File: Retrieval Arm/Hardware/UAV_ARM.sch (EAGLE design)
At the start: 20 parts, among them Q1 Q_ATMEGA328P, Q2 Q_LTC490, Q3 Q_LDO, X1 X_HC49SCRYSTAL

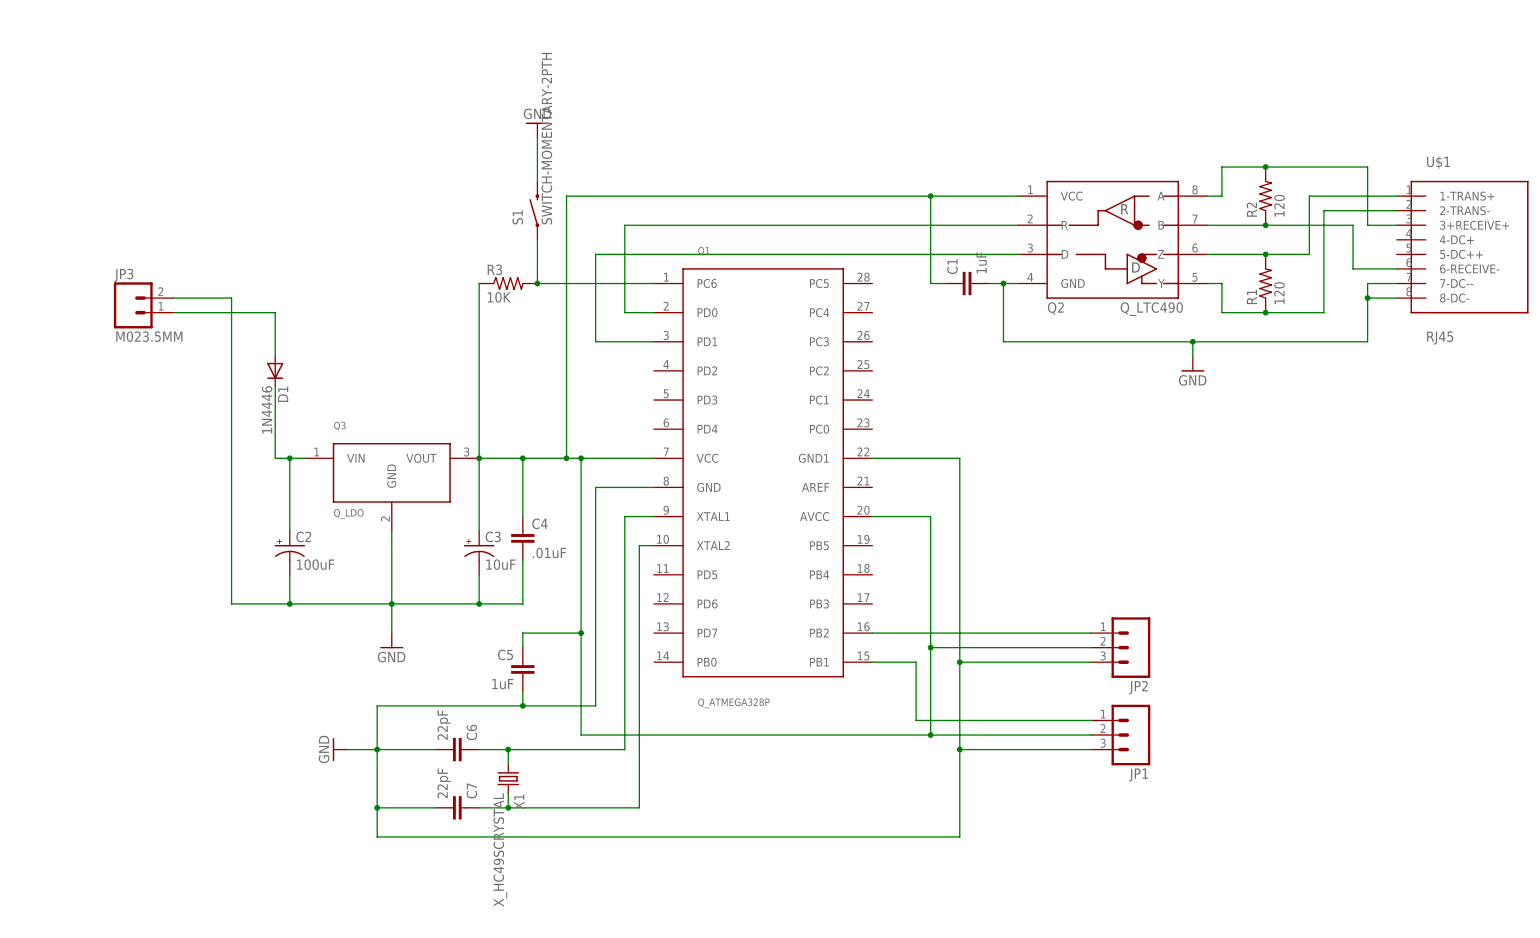
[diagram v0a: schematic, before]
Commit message: Redesigned for new arm
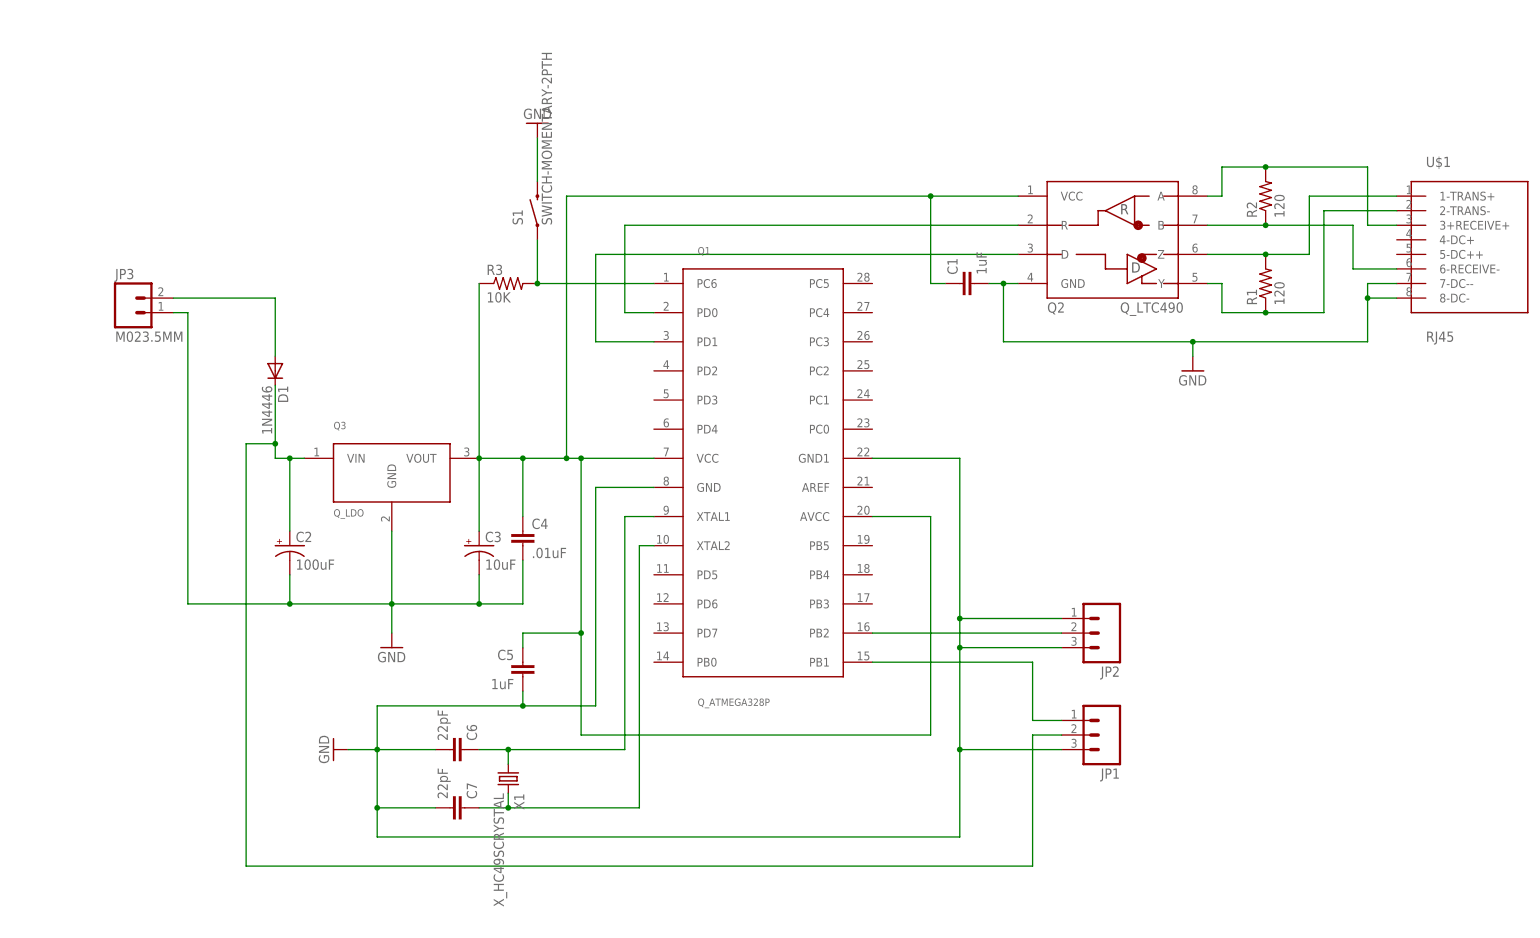
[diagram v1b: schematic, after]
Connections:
- removed net N$12: JP2.1, Q1.PB2
- removed net N$14 (its old number): C1.1, C3.+, C4.1, C5.1, JP1.2, JP2.2, Q1.AVCC, Q1.VCC, Q2.VCC, Q3.VOUT, R3.1
- new net N$15: D1.A, JP3.2
- new net N$6: C1.1, C3.+, C4.1, C5.1, Q1.AVCC, Q1.VCC, Q2.VCC, Q3.VOUT, R3.1
- net GND: now also JP2.1, JP3.1; no longer JP3.2
- net N$13: now also JP2.2, Q1.PB2; no longer D1.A, JP3.1
- net N$5: now also JP1.2
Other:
- moved on the sheet: JP1, JP2
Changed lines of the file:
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@@
 <part name="X1" library="MRDT-2014-All" deviceset="X_HC49SCRYSTAL" device=""/>
 <part name="GND4" library="supply1" deviceset="GND" device=""/>
+<part name="JP3" library="SparkFun-Connectors" deviceset="M02" device="3.5MM"/>
+<part name="S1" library="SparkFun-Electromechanical" deviceset="SWITCH-MOMENTARY-2" device="PTH"/>
 <part name="JP1" library="SparkFun-Connectors" deviceset="M03" device="POLAR"/>
 <part name="JP2" library="SparkFun-Connectors" deviceset="M03" device="POLAR"/>
-<part name="JP3" library="SparkFun-Connectors" deviceset="M02" device="3.5MM"/>
-<part name="S1" library="SparkFun-Electromechanical" deviceset="SWITCH-MOMENTARY-2" device="PTH"/>
 </parts>
 <sheets>
@@
 <instance part="X1" gate="G$1" x="43.18" y="-20.32" rot="R270"/>
 <instance part="GND4" gate="1" x="12.7" y="-15.24" rot="R270"/>
-<instance part="JP1" gate="G$1" x="152.4" y="-12.7" rot="R180"/>
-<instance part="JP2" gate="G$1" x="152.4" y="2.54" rot="R180"/>
 <instance part="JP3" gate="G$1" x="-22.86" y="60.96"/>
 <instance part="S1" gate="G$1" x="48.26" y="78.74" rot="R90"/>
+<instance part="JP1" gate="G$1" x="147.32" y="-12.7" rot="R180"/>
+<instance part="JP2" gate="G$1" x="147.32" y="5.08" rot="R180"/>
 </instances>
 <busses>
@@
 <junction x="38.1" y="10.16"/>
 <junction x="22.86" y="10.16"/>
-<wire x1="5.08" y1="10.16" x2="-5.08" y2="10.16" width="0.1524" layer="91"/>
-<wire x1="-5.08" y1="10.16" x2="-5.08" y2="63.5" width="0.1524" layer="91"/>
-<pinref part="JP3" gate="G$1" pin="2"/>
-<wire x1="-15.24" y1="63.5" x2="-5.08" y2="63.5" width="0.1524" layer="91"/>
+<wire x1="5.08" y1="10.16" x2="-12.7" y2="10.16" width="0.1524" layer="91"/>
 <junction x="5.08" y="10.16"/>
+<wire x1="-12.7" y1="10.16" x2="-12.7" y2="60.96" width="0.1524" layer="91"/>
+<pinref part="JP3" gate="G$1" pin="1"/>
+<wire x1="-12.7" y1="60.96" x2="-15.24" y2="60.96" width="0.1524" layer="91"/>
 </segment>
 <segment>
@@
 <pinref part="Q1" gate="G$1" pin="GND1"/>
 <wire x1="106.68" y1="35.56" x2="121.92" y2="35.56" width="0.1524" layer="91"/>
-<wire x1="121.92" y1="35.56" x2="121.92" y2="0" width="0.1524" layer="91"/>
-<wire x1="121.92" y1="0" x2="121.92" y2="-15.24" width="0.1524" layer="91"/>
+<wire x1="121.92" y1="35.56" x2="121.92" y2="7.62" width="0.1524" layer="91"/>
+<wire x1="121.92" y1="7.62" x2="121.92" y2="2.54" width="0.1524" layer="91"/>
+<wire x1="121.92" y1="2.54" x2="121.92" y2="-15.24" width="0.1524" layer="91"/>
 <wire x1="121.92" y1="-15.24" x2="121.92" y2="-30.48" width="0.1524" layer="91"/>
 <wire x1="121.92" y1="-30.48" x2="20.32" y2="-30.48" width="0.1524" layer="91"/>
 <wire x1="20.32" y1="-30.48" x2="20.32" y2="-25.4" width="0.1524" layer="91"/>
 <junction x="20.32" y="-25.4"/>
-<pinref part="JP2" gate="G$1" pin="3"/>
-<wire x1="144.78" y1="0" x2="121.92" y2="0" width="0.1524" layer="91"/>
-<pinref part="JP1" gate="G$1" pin="3"/>
-<wire x1="144.78" y1="-15.24" x2="121.92" y2="-15.24" width="0.1524" layer="91"/>
-<junction x="121.92" y="-15.24"/>
-<junction x="121.92" y="0"/>
 <pinref part="C5" gate="G$1" pin="2"/>
 <wire x1="20.32" y1="-7.62" x2="45.72" y2="-7.62" width="0.1524" layer="91"/>
@@
 <wire x1="45.72" y1="-7.62" x2="58.42" y2="-7.62" width="0.1524" layer="91"/>
 <junction x="45.72" y="-7.62"/>
-</segment>
-</net>
-<net name="N$5" class="0">
-<segment>
-<pinref part="Q3" gate="G$1" pin="VIN"/>
-<pinref part="D1" gate="1" pin="C"/>
-<wire x1="7.62" y1="35.56" x2="5.08" y2="35.56" width="0.1524" layer="91"/>
-<wire x1="5.08" y1="35.56" x2="2.54" y2="35.56" width="0.1524" layer="91"/>
-<wire x1="2.54" y1="35.56" x2="2.54" y2="48.26" width="0.1524" layer="91"/>
-<pinref part="C2" gate="G$1" pin="+"/>
-<wire x1="5.08" y1="22.86" x2="5.08" y2="35.56" width="0.1524" layer="91"/>
-<junction x="5.08" y="35.56"/>
+<wire x1="139.7" y1="-15.24" x2="121.92" y2="-15.24" width="0.1524" layer="91"/>
+<junction x="121.92" y="-15.24"/>
+<pinref part="JP1" gate="G$1" pin="3"/>
+<wire x1="139.7" y1="2.54" x2="121.92" y2="2.54" width="0.1524" layer="91"/>
+<pinref part="JP2" gate="G$1" pin="1"/>
+<wire x1="139.7" y1="7.62" x2="121.92" y2="7.62" width="0.1524" layer="91"/>
+<junction x="121.92" y="2.54"/>
+<junction x="121.92" y="7.62"/>
+<pinref part="JP2" gate="G$1" pin="3"/>
 </segment>
 </net>
@@
 </segment>
 </net>
-<net name="N$16" class="0">
-<segment>
-<pinref part="JP1" gate="G$1" pin="1"/>
-<wire x1="144.78" y1="-10.16" x2="114.3" y2="-10.16" width="0.1524" layer="91"/>
-<wire x1="114.3" y1="-10.16" x2="114.3" y2="0" width="0.1524" layer="91"/>
-<pinref part="Q1" gate="G$1" pin="PB1"/>
-<wire x1="114.3" y1="0" x2="106.68" y2="0" width="0.1524" layer="91"/>
-</segment>
-</net>
-<net name="N$12" class="0">
-<segment>
-<pinref part="JP2" gate="G$1" pin="1"/>
-<pinref part="Q1" gate="G$1" pin="PB2"/>
-<wire x1="144.78" y1="5.08" x2="106.68" y2="5.08" width="0.1524" layer="91"/>
-</segment>
-</net>
-<net name="N$13" class="0">
-<segment>
-<pinref part="D1" gate="1" pin="A"/>
-<wire x1="-15.24" y1="60.96" x2="2.54" y2="60.96" width="0.1524" layer="91"/>
-<wire x1="2.54" y1="60.96" x2="2.54" y2="53.34" width="0.1524" layer="91"/>
-<pinref part="JP3" gate="G$1" pin="1"/>
-</segment>
-</net>
 <net name="N$8" class="0">
 <segment>
@@
 </segment>
 </net>
-<net name="N$14" class="0">
+<net name="N$6" class="0">
 <segment>
 <pinref part="C5" gate="G$1" pin="1"/>
@@
 <pinref part="Q1" gate="G$1" pin="AVCC"/>
 <wire x1="106.68" y1="25.4" x2="116.84" y2="25.4" width="0.1524" layer="91"/>
-<wire x1="116.84" y1="25.4" x2="116.84" y2="2.54" width="0.1524" layer="91"/>
-<pinref part="JP2" gate="G$1" pin="2"/>
-<wire x1="144.78" y1="2.54" x2="116.84" y2="2.54" width="0.1524" layer="91"/>
-<junction x="116.84" y="2.54"/>
-<wire x1="116.84" y1="2.54" x2="116.84" y2="-12.7" width="0.1524" layer="91"/>
-<pinref part="JP1" gate="G$1" pin="2"/>
-<wire x1="144.78" y1="-12.7" x2="116.84" y2="-12.7" width="0.1524" layer="91"/>
-<junction x="116.84" y="-12.7"/>
+<wire x1="116.84" y1="25.4" x2="116.84" y2="-12.7" width="0.1524" layer="91"/>
 <wire x1="116.84" y1="-12.7" x2="55.88" y2="-12.7" width="0.1524" layer="91"/>
 <wire x1="55.88" y1="-12.7" x2="55.88" y2="5.08" width="0.1524" layer="91"/>
@@
 <wire x1="38.1" y1="66.04" x2="38.1" y2="35.56" width="0.1524" layer="91"/>
 <wire x1="53.34" y1="81.28" x2="53.34" y2="35.56" width="0.1524" layer="91"/>
-<pinref part="Q2" gate="G$1" pin="VCC"/>
-<wire x1="53.34" y1="81.28" x2="116.84" y2="81.28" width="0.1524" layer="91"/>
-<pinref part="C1" gate="G$1" pin="1"/>
-<wire x1="116.84" y1="81.28" x2="132.08" y2="81.28" width="0.1524" layer="91"/>
-<wire x1="119.38" y1="66.04" x2="116.84" y2="66.04" width="0.1524" layer="91"/>
-<wire x1="116.84" y1="66.04" x2="116.84" y2="81.28" width="0.1524" layer="91"/>
-<junction x="116.84" y="81.28"/>
 <wire x1="55.88" y1="5.08" x2="55.88" y2="35.56" width="0.1524" layer="91"/>
 <junction x="55.88" y="35.56"/>
 <junction x="55.88" y="5.08"/>
+<pinref part="C1" gate="G$1" pin="1"/>
+<wire x1="119.38" y1="66.04" x2="116.84" y2="66.04" width="0.1524" layer="91"/>
+<wire x1="116.84" y1="66.04" x2="116.84" y2="81.28" width="0.1524" layer="91"/>
+<pinref part="Q2" gate="G$1" pin="VCC"/>
+<wire x1="116.84" y1="81.28" x2="132.08" y2="81.28" width="0.1524" layer="91"/>
+<wire x1="53.34" y1="81.28" x2="116.84" y2="81.28" width="0.1524" layer="91"/>
+<junction x="116.84" y="81.28"/>
+</segment>
+</net>
+<net name="N$13" class="0">
+<segment>
+<pinref part="JP2" gate="G$1" pin="2"/>
+<pinref part="Q1" gate="G$1" pin="PB2"/>
+<wire x1="139.7" y1="5.08" x2="106.68" y2="5.08" width="0.1524" layer="91"/>
+</segment>
+</net>
+<net name="N$14" class="0">
+<segment>
+<pinref part="Q1" gate="G$1" pin="PB1"/>
+<wire x1="106.68" y1="0" x2="134.62" y2="0" width="0.1524" layer="91"/>
+<wire x1="134.62" y1="0" x2="134.62" y2="-10.16" width="0.1524" layer="91"/>
+<pinref part="JP1" gate="G$1" pin="1"/>
+<wire x1="134.62" y1="-10.16" x2="139.7" y2="-10.16" width="0.1524" layer="91"/>
+</segment>
+</net>
+<net name="N$15" class="0">
+<segment>
+<pinref part="D1" gate="1" pin="A"/>
+<wire x1="2.54" y1="63.5" x2="2.54" y2="53.34" width="0.1524" layer="91"/>
+<pinref part="JP3" gate="G$1" pin="2"/>
+<wire x1="-15.24" y1="63.5" x2="2.54" y2="63.5" width="0.1524" layer="91"/>
+</segment>
+</net>
+<net name="N$5" class="0">
+<segment>
+<wire x1="139.7" y1="-12.7" x2="134.62" y2="-12.7" width="0.1524" layer="91"/>
+<wire x1="134.62" y1="-12.7" x2="134.62" y2="-35.56" width="0.1524" layer="91"/>
+<wire x1="134.62" y1="-35.56" x2="-2.54" y2="-35.56" width="0.1524" layer="91"/>
+<pinref part="JP1" gate="G$1" pin="2"/>
+<wire x1="-2.54" y1="-35.56" x2="-2.54" y2="38.1" width="0.1524" layer="91"/>
+<pinref part="Q3" gate="G$1" pin="VIN"/>
+<pinref part="D1" gate="1" pin="C"/>
+<wire x1="7.62" y1="35.56" x2="5.08" y2="35.56" width="0.1524" layer="91"/>
+<wire x1="5.08" y1="35.56" x2="2.54" y2="35.56" width="0.1524" layer="91"/>
+<wire x1="2.54" y1="35.56" x2="2.54" y2="38.1" width="0.1524" layer="91"/>
+<pinref part="C2" gate="G$1" pin="+"/>
+<wire x1="2.54" y1="38.1" x2="2.54" y2="48.26" width="0.1524" layer="91"/>
+<wire x1="5.08" y1="22.86" x2="5.08" y2="35.56" width="0.1524" layer="91"/>
+<junction x="5.08" y="35.56"/>
+<wire x1="-2.54" y1="38.1" x2="2.54" y2="38.1" width="0.1524" layer="91"/>
+<junction x="2.54" y="38.1"/>
 </segment>
 </net>
@@
 </sheet>
 </sheets>
-<errors>
-</errors>
 </schematic>
 </drawing>

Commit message: I am taking over electronics hardware development
The previous board was literally the worst PCB i’ve ever seen. EAGLE’s
autorouter should not be used under any circumstances. I can be quoted
on both of these statements, and will not apologize for either.

That being said, I redesigned the entire board using the 32u4 Breakout
board, proper SMT, proper layout, intelligent routing, PoRC Spec, and a
visually symmetrical design. The design should still be checked, as the
connections used are not necessarily correct.
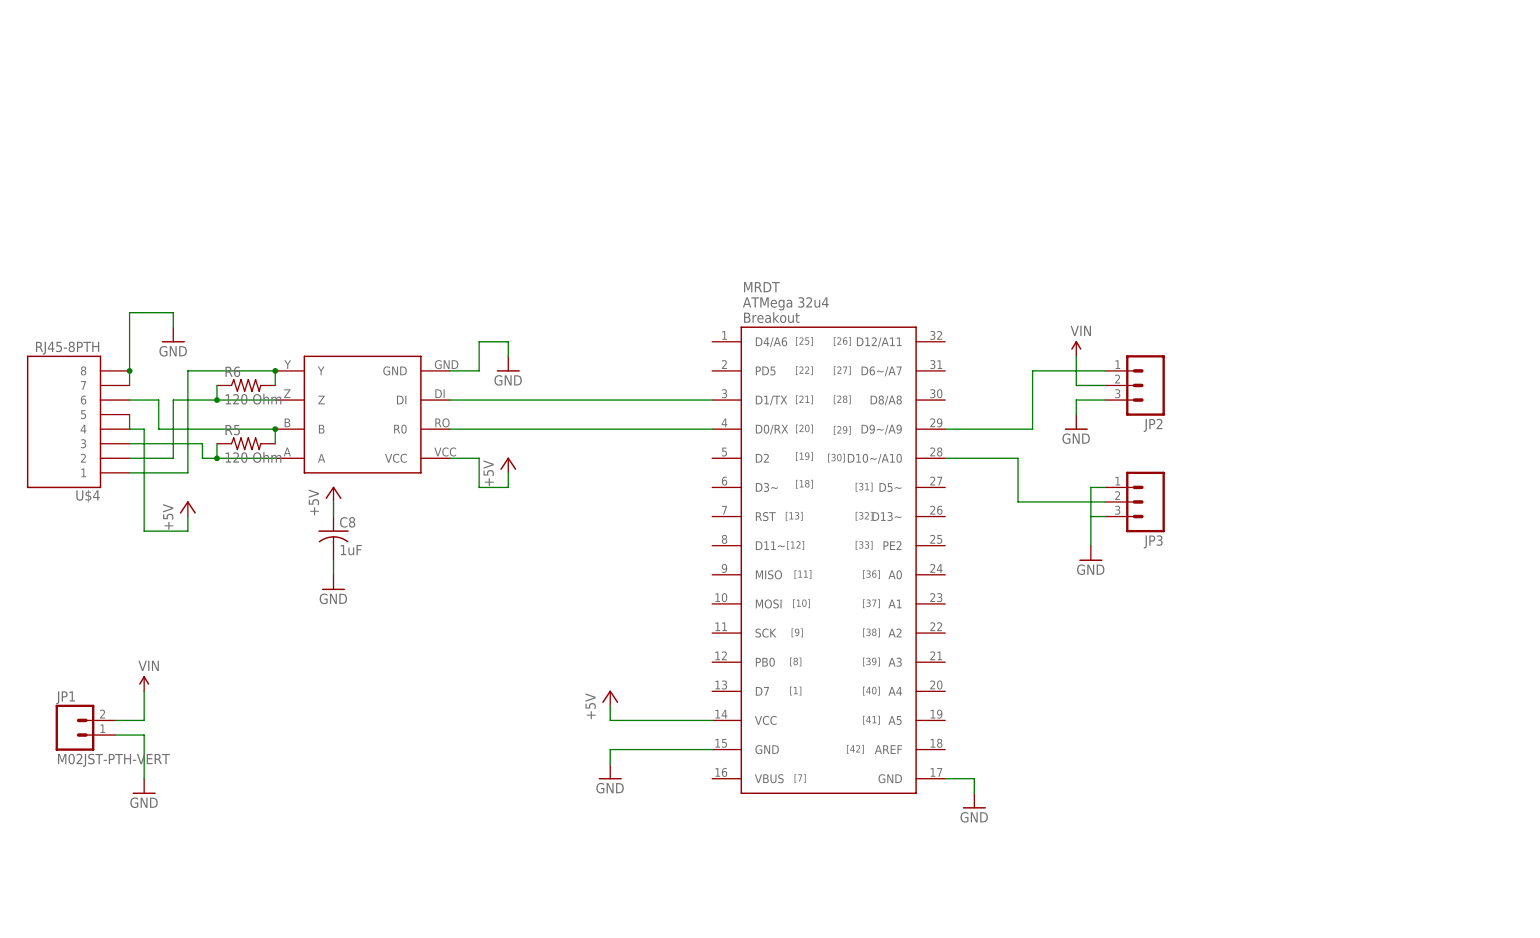
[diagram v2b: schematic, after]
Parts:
- removed C1, C5: 1uF, SparkFun-Capacitors:CAPKIT
- removed C2: 100uF, SparkFun-Passives:CAP_POLPTH1
- removed C3: 10uF, SparkFun-Passives:CAP_POLPTH2
- removed C4: .01uF, SparkFun-Capacitors:CAPKIT
- removed C6, C7: 22pF, SparkFun-Capacitors:CAPKIT
- removed D1: 1N4446, diode:1N4446
- removed Q1: Q_ATMEGA328P, MRDT-2014-All:Q_ATMEGA328P
- removed Q2: Q_LTC490, MRDT-2014-All:Q_LTC490
- removed Q3: Q_LDO, MRDT-2015-General:Q_LDO
- removed R1, R2: 120, resistor:R-US_0204/7
- removed R3: 10K, resistor:R-US_0204/7
- removed S1: SWITCH-MOMENTARY-2PTH, SparkFun-Electromechanical:SWITCH-MOMENTARY-2PTH
- removed U$1: RJ45, MRDT-2014-All:RJ45
- removed X1: X_HC49SCRYSTAL, MRDT-2014-All:X_HC49SCRYSTAL
- added C8: 1uF, resistor:C-USC1206
- added R5, R6: 120 Ohm, SparkFun-Passives:RESISTOR1206
- added U$2: 32U4_BREAKOUT, MRDT-2015-General:32U4_BREAKOUT
- added U$3: MAX3077, MAX3077:MAX3077
- added U$4: RJ45-8PTH, SparkFun-Connectors:RJ45-8PTH
- JP1: value (none) -> M02JST-PTH-VERT; device SparkFun-Connectors:M03POLAR -> SparkFun-Connectors:M02JST-PTH-VERT
- JP2: device SparkFun-Connectors:M03POLAR -> SparkFun-Connectors:M03JST-PTH
- JP3: value M023.5MM -> (none); device SparkFun-Connectors:M023.5MM -> SparkFun-Connectors:M03JST-PTH
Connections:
- removed net N$10: C6.1, Q1.XTAL1, X1.1
- removed net N$11: C7.1, Q1.XTAL2, X1.2
- removed net N$13: JP2.2, Q1.PB2
- removed net N$14: JP1.1, Q1.PB1
- removed net N$15: D1.A, JP3.2
- removed net N$3: Q2.Y, R1.1, U$1.2-TRANS-
- removed net N$4: Q2.Z, R1.2, U$1.1-TRANS+
- removed net N$5: C2.+, D1.C, JP1.2, Q3.VIN
- removed net N$6: C1.1, C3.+, C4.1, C5.1, Q1.AVCC, Q1.VCC, Q2.VCC, Q3.VOUT, R3.1
- removed net N$7: Q1.PD1, Q2.D
- removed net N$8: Q1.PD0, Q2.R
- removed net N$9: Q1.PC6, R3.2, S1.1
- new net +5V: C8.1, U$2.VCC, U$3.VCC, U$4.4, U$4.5
- new net N$12: R6.2, U$3.Y, U$4.1
- new net N$18: R6.1, U$3.Z, U$4.2
- new net N$19: R5.2, U$3.B, U$4.6
- new net N$20: R5.1, U$3.A, U$4.3
- new net N$21: U$2.D1/TX, U$3.DI
- new net RXD: U$2.D0/RX, U$3.R0
- new net VIN: JP1.2, JP2.2
- net GND: now also C8.2, JP1.1, JP3.3, U$2.GND@1, U$2.GND@2, U$3.GND, U$4.7, U$4.8; no longer C1.2, C2.-, C3.-, C4.2, C5.2, C6.2, C7.2, JP1.3, JP2.1, Q1.GND, Q1.GND1, Q2.GND, Q3.GND, S1.2, U$1.7-DC--, U$1.8-DC-
- net N$1: now also JP3.2, U$2.D10~/A10; no longer Q2.A, R2.2, U$1.3+RECEIVE+
- net N$2: now also JP2.1, U$2.D9~/A9; no longer Q2.B, R2.1, U$1.6-RECEIVE-
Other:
- moved on the sheet: JP2
